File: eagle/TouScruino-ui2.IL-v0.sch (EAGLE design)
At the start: 7 parts

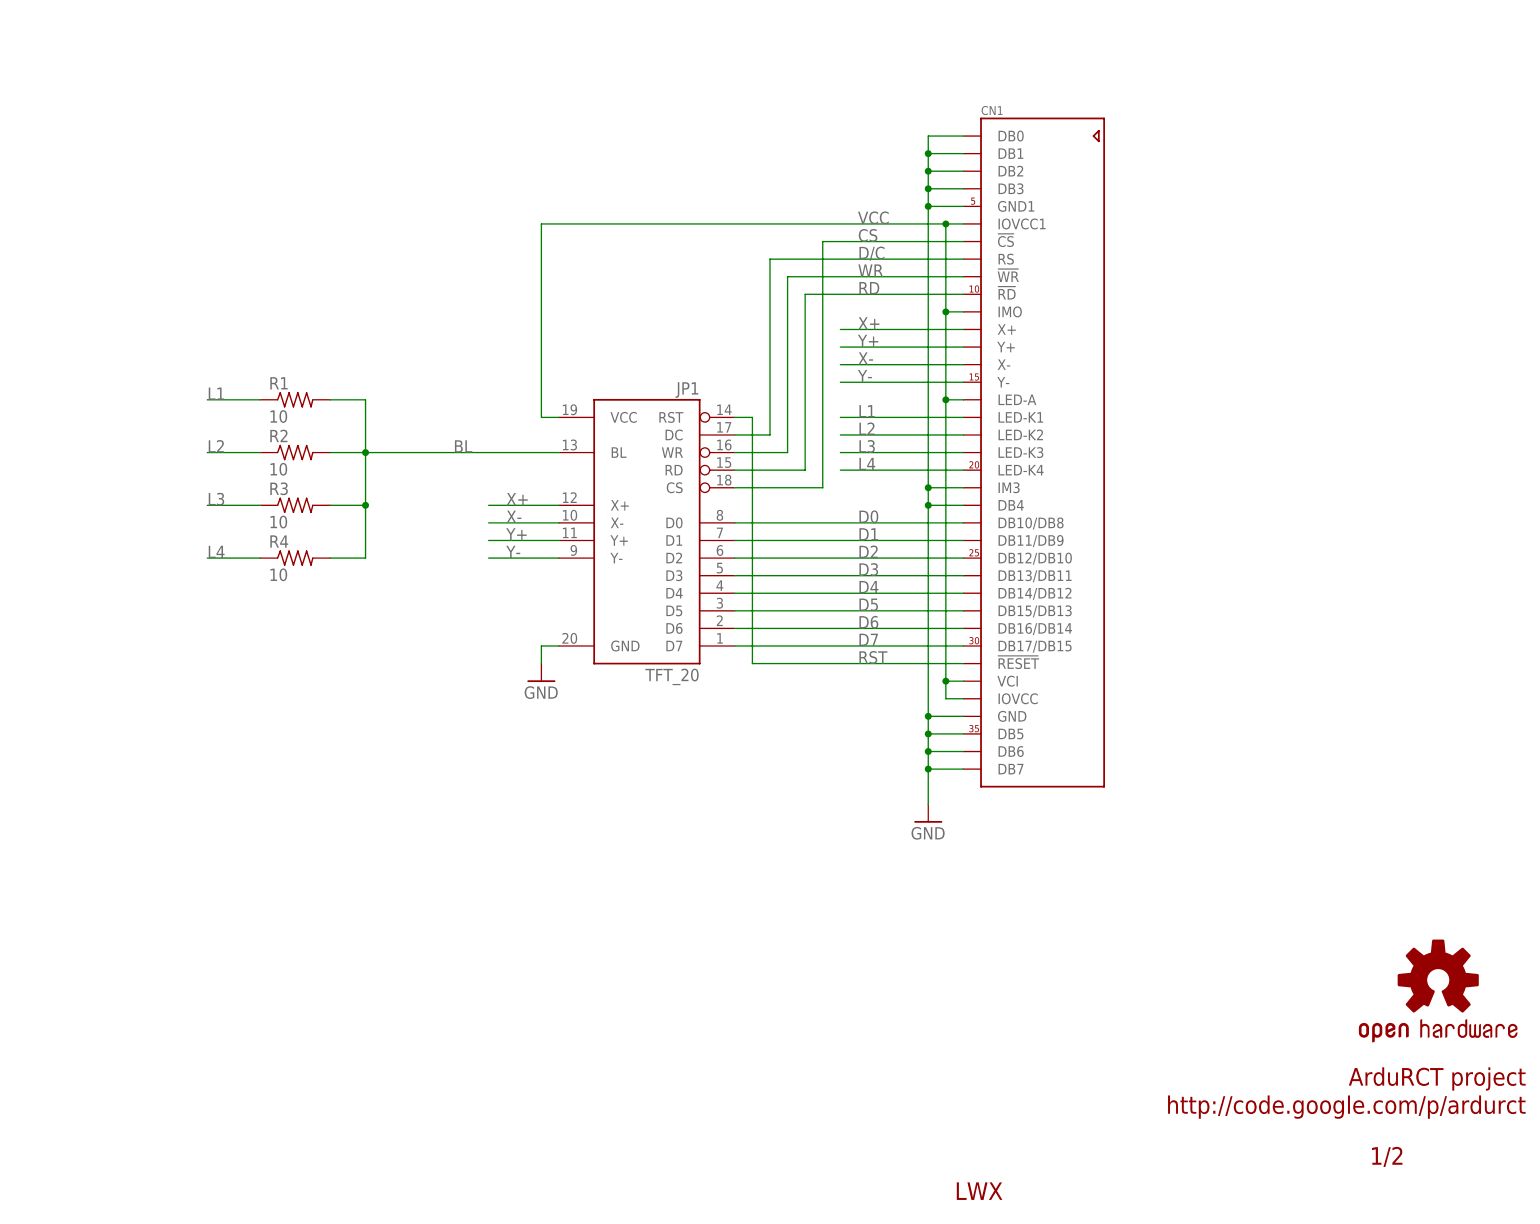
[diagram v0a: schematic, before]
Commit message: 
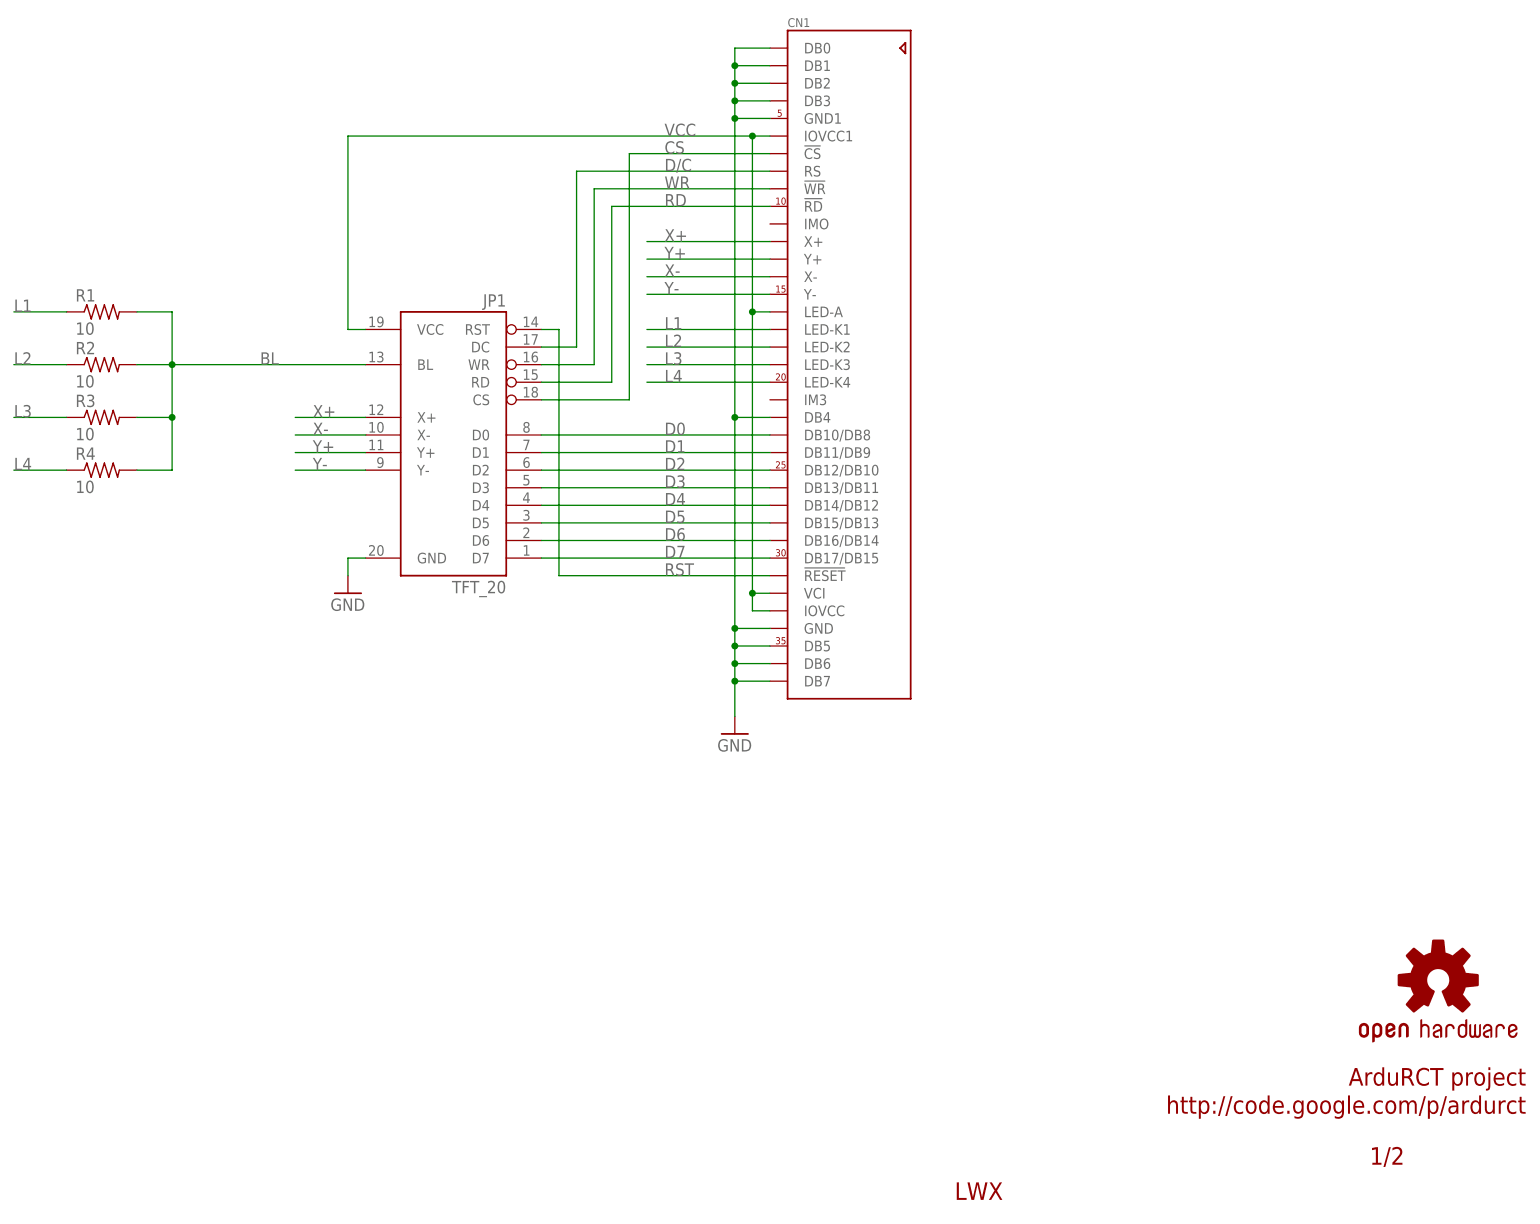
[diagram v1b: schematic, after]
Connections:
- net GND: no longer CN1.IM3
- net VCC: no longer CN1.IMO
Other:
- moved on the sheet: CN1, JP1, R1, R2, R3, R4
